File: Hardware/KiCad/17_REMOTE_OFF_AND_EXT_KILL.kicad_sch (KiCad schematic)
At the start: 0 parts

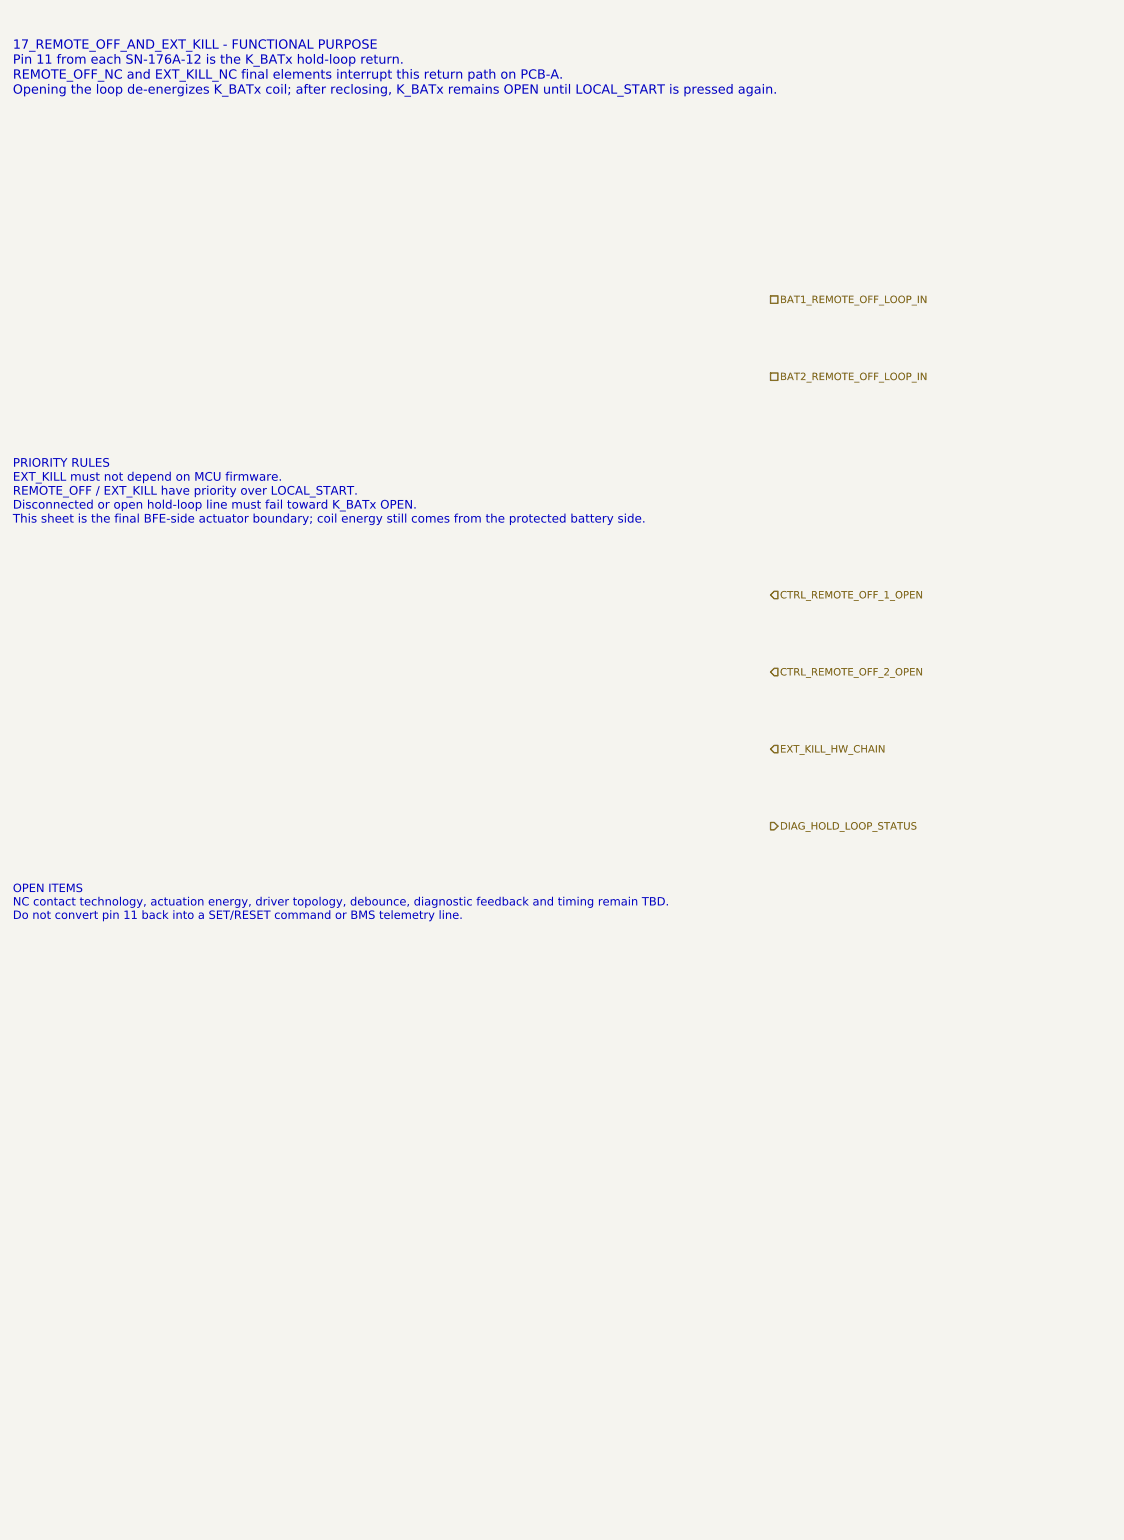
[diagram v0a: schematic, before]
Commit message: hardware: refine REMOTE_OFF and EXT_KILL hold-loop level B
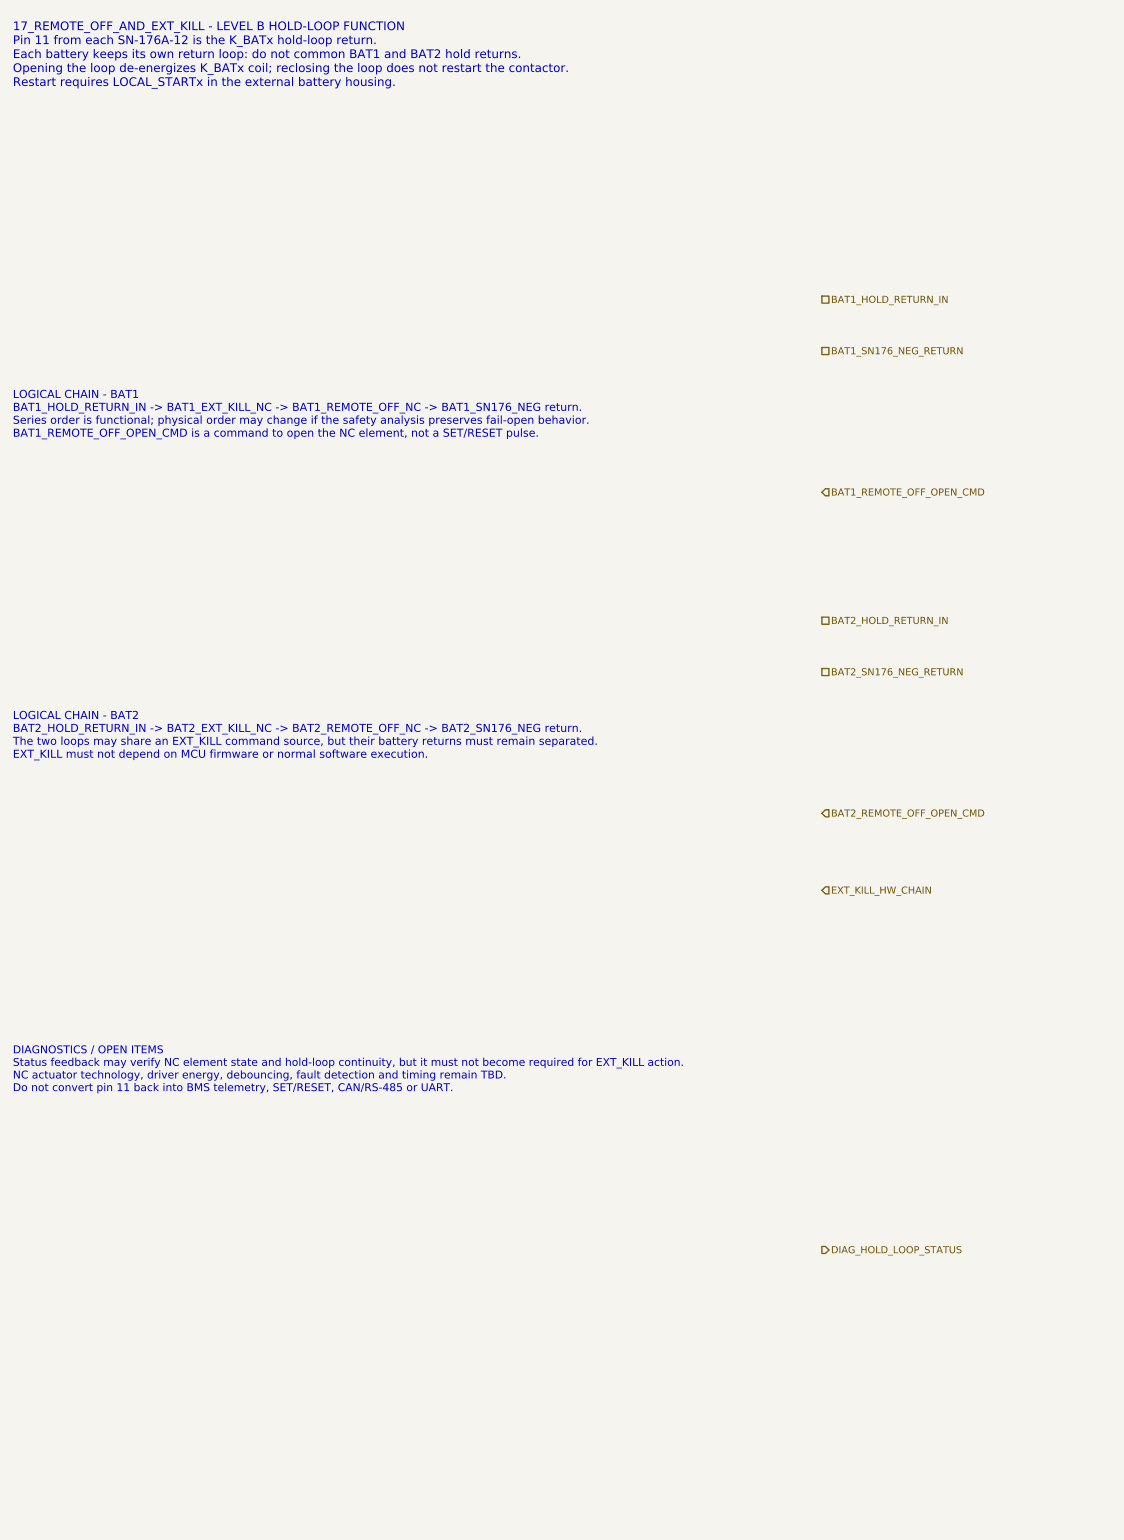
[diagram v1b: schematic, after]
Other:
- note added: "17_REMOTE_OFF_AND_EXT_KILL - LEVEL B HOLD-LOOP FUNCTION Pin 11 from each SN-176A-12 is the K_BATx hold-loop return. Each battery keeps its own return loop: do not common BAT1 and BAT2 hold returns. Opening the loop de-energizes K_BATx coil; reclosing the loop does not restart the contactor. Restart requires LOCAL_STARTx in the external battery housing."
- note added: "DIAGNOSTICS / OPEN ITEMS Status feedback may verify NC element state and hold-loop continuity, but it must not become required for EXT_KILL action. NC actuator technology, driver energy, debouncing, fault detection and timing remain TBD. Do not convert pin 11 back into BMS telemetry, SET/RESET, CAN/RS-485 or UART."
- note added: "LOGICAL CHAIN - BAT1 BAT1_HOLD_RETURN_IN -> BAT1_EXT_KILL_NC -> BAT1_REMOTE_OFF_NC -> BAT1_SN176_NEG return. Series order is functional; physical order may change if the safety analysis preserves fail-open behavior. BAT1_REMOTE_OFF_OPEN_CMD is a command to open the NC element, not a SET/RESET pulse."
- note added: "LOGICAL CHAIN - BAT2 BAT2_HOLD_RETURN_IN -> BAT2_EXT_KILL_NC -> BAT2_REMOTE_OFF_NC -> BAT2_SN176_NEG return. The two loops may share an EXT_KILL command source, but their battery returns must remain separated. EXT_KILL must not depend on MCU firmware or normal software execution."
- note removed: "17_REMOTE_OFF_AND_EXT_KILL - FUNCTIONAL PURPOSE Pin 11 from each SN-176A-12 is the K_BATx hold-loop return. REMOTE_OFF_NC and EXT_KILL_NC final elements interrupt this return path on PCB-A. Opening the loop de-energizes K_BATx coil; after reclosing, K_BATx remains OPEN until LOCAL_START is pressed again."
- note removed: "OPEN ITEMS NC contact technology, actuation energy, driver topology, debounce, diagnostic feedback and timing remain TBD. Do not convert pin 11 back into a SET/RESET command or BMS telemetry line."
- note removed: "PRIORITY RULES EXT_KILL must not depend on MCU firmware. REMOTE_OFF / EXT_KILL have priority over LOCAL_START. Disconnected or open hold-loop line must fail toward K_BATx OPEN. This sheet is the final BFE-side actuator boundary; coil energy still comes from the protected battery side."
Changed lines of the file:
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@@
 		(title "17_REMOTE_OFF_AND_EXT_KILL - hold-loop final actuators")
 		(date "2026-07-15")
-		(rev "A1")
+		(rev "B1")
 		(company "Gonoboben/plataVM")
-		(comment 1 "Architecture Level A: REMOTE_OFF_NC and EXT_KILL_NC boundary")
+		(comment 1 "Architecture Level B: hold-loop return interruption and safe-state rules")
 		(comment 2 "No relay/MOSFET/contact implementation selected")
 	)
-	(text "17_REMOTE_OFF_AND_EXT_KILL - FUNCTIONAL PURPOSE\nPin 11 from each SN-176A-12 is the K_BATx hold-loop return.\nREMOTE_OFF_NC and EXT_KILL_NC final elements interrupt this return path on PCB-A.\nOpening the loop de-energizes K_BATx coil; after reclosing, K_BATx remains OPEN until LOCAL_START is pressed again."
+	(text "17_REMOTE_OFF_AND_EXT_KILL - LEVEL B HOLD-LOOP FUNCTION\nPin 11 from each SN-176A-12 is the K_BATx hold-loop return.\nEach battery keeps its own return loop: do not common BAT1 and BAT2 hold returns.\nOpening the loop de-energizes K_BATx coil; reclosing the loop does not restart the contactor.\nRestart requires LOCAL_STARTx in the external battery housing."
 		(exclude_from_sim no)
-		(at 12 18 0)
-		(effects (font (size 1.45 1.45)) (justify left))
+		(at 12 16 0)
+		(effects (font (size 1.35 1.35)) (justify left))
 		(uuid "bfe-dh-00000017-0000-4000-8000-000000000101")
 	)
-	(text "PRIORITY RULES\nEXT_KILL must not depend on MCU firmware.\nREMOTE_OFF / EXT_KILL have priority over LOCAL_START.\nDisconnected or open hold-loop line must fail toward K_BATx OPEN.\nThis sheet is the final BFE-side actuator boundary; coil energy still comes from the protected battery side."
+	(text "LOGICAL CHAIN - BAT1\nBAT1_HOLD_RETURN_IN -> BAT1_EXT_KILL_NC -> BAT1_REMOTE_OFF_NC -> BAT1_SN176_NEG return.\nSeries order is functional; physical order may change if the safety analysis preserves fail-open behavior.\nBAT1_REMOTE_OFF_OPEN_CMD is a command to open the NC element, not a SET/RESET pulse."
 		(exclude_from_sim no)
-		(at 12 84 0)
-		(effects (font (size 1.35 1.35)) (justify left))
+		(at 12 72 0)
+		(effects (font (size 1.25 1.25)) (justify left))
 		(uuid "bfe-dh-00000017-0000-4000-8000-000000000102")
 	)
-	(text "OPEN ITEMS\nNC contact technology, actuation energy, driver topology, debounce, diagnostic feedback and timing remain TBD.\nDo not convert pin 11 back into a SET/RESET command or BMS telemetry line."
+	(text "LOGICAL CHAIN - BAT2\nBAT2_HOLD_RETURN_IN -> BAT2_EXT_KILL_NC -> BAT2_REMOTE_OFF_NC -> BAT2_SN176_NEG return.\nThe two loops may share an EXT_KILL command source, but their battery returns must remain separated.\nEXT_KILL must not depend on MCU firmware or normal software execution."
 		(exclude_from_sim no)
-		(at 12 148 0)
-		(effects (font (size 1.3 1.3)) (justify left))
+		(at 12 122 0)
+		(effects (font (size 1.25 1.25)) (justify left))
 		(uuid "bfe-dh-00000017-0000-4000-8000-000000000103")
 	)
-	(hierarchical_label "BAT1_REMOTE_OFF_LOOP_IN" (shape passive) (exclude_from_sim no) (at 130 54 0) (effects (font (size 1.15 1.15)) (justify left)) (uuid "bfe-dh-00000017-0000-4000-8000-000000000201"))
-	(hierarchical_label "BAT2_REMOTE_OFF_LOOP_IN" (shape passive) (exclude_from_sim no) (at 130 66 0) (effects (font (size 1.15 1.15)) (justify left)) (uuid "bfe-dh-00000017-0000-4000-8000-000000000202"))
-	(hierarchical_label "CTRL_REMOTE_OFF_1_OPEN" (shape input) (exclude_from_sim no) (at 130 100 0) (effects (font (size 1.15 1.15)) (justify left)) (uuid "bfe-dh-00000017-0000-4000-8000-000000000203"))
-	(hierarchical_label "CTRL_REMOTE_OFF_2_OPEN" (shape input) (exclude_from_sim no) (at 130 112 0) (effects (font (size 1.15 1.15)) (justify left)) (uuid "bfe-dh-00000017-0000-4000-8000-000000000204"))
-	(hierarchical_label "EXT_KILL_HW_CHAIN" (shape input) (exclude_from_sim no) (at 130 124 0) (effects (font (size 1.15 1.15)) (justify left)) (uuid "bfe-dh-00000017-0000-4000-8000-000000000205"))
-	(hierarchical_label "DIAG_HOLD_LOOP_STATUS" (shape output) (exclude_from_sim no) (at 130 136 0) (effects (font (size 1.15 1.15)) (justify left)) (uuid "bfe-dh-00000017-0000-4000-8000-000000000206"))
+	(text "DIAGNOSTICS / OPEN ITEMS\nStatus feedback may verify NC element state and hold-loop continuity, but it must not become required for EXT_KILL action.\nNC actuator technology, driver energy, debouncing, fault detection and timing remain TBD.\nDo not convert pin 11 back into BMS telemetry, SET/RESET, CAN/RS-485 or UART."
+		(exclude_from_sim no)
+		(at 12 174 0)
+		(effects (font (size 1.22 1.22)) (justify left))
+		(uuid "bfe-dh-00000017-0000-4000-8000-000000000104")
+	)
+	(hierarchical_label "BAT1_HOLD_RETURN_IN" (shape passive) (exclude_from_sim no) (at 138 54 0) (effects (font (size 1.1 1.1)) (justify left)) (uuid "bfe-dh-00000017-0000-4000-8000-000000000201"))
+	(hierarchical_label "BAT1_SN176_NEG_RETURN" (shape passive) (exclude_from_sim no) (at 138 62 0) (effects (font (size 1.1 1.1)) (justify left)) (uuid "bfe-dh-00000017-0000-4000-8000-000000000202"))
+	(hierarchical_label "BAT2_HOLD_RETURN_IN" (shape passive) (exclude_from_sim no) (at 138 104 0) (effects (font (size 1.1 1.1)) (justify left)) (uuid "bfe-dh-00000017-0000-4000-8000-000000000203"))
+	(hierarchical_label "BAT2_SN176_NEG_RETURN" (shape passive) (exclude_from_sim no) (at 138 112 0) (effects (font (size 1.1 1.1)) (justify left)) (uuid "bfe-dh-00000017-0000-4000-8000-000000000204"))
+	(hierarchical_label "BAT1_REMOTE_OFF_OPEN_CMD" (shape input) (exclude_from_sim no) (at 138 84 0) (effects (font (size 1.1 1.1)) (justify left)) (uuid "bfe-dh-00000017-0000-4000-8000-000000000205"))
+	(hierarchical_label "BAT2_REMOTE_OFF_OPEN_CMD" (shape input) (exclude_from_sim no) (at 138 134 0) (effects (font (size 1.1 1.1)) (justify left)) (uuid "bfe-dh-00000017-0000-4000-8000-000000000206"))
+	(hierarchical_label "EXT_KILL_HW_CHAIN" (shape input) (exclude_from_sim no) (at 138 146 0) (effects (font (size 1.1 1.1)) (justify left)) (uuid "bfe-dh-00000017-0000-4000-8000-000000000207"))
+	(hierarchical_label "DIAG_HOLD_LOOP_STATUS" (shape output) (exclude_from_sim no) (at 138 202 0) (effects (font (size 1.1 1.1)) (justify left)) (uuid "bfe-dh-00000017-0000-4000-8000-000000000208"))
 )
